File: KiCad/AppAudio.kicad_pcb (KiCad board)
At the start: 2 copper layers, 60 x 62 mm, 34 parts, among them P1 WRITER-VCC, Q1 Q_NMOS_SGD, SW1 SW_PUSH, SW2 SW_PUSH, U1 TWE_LITE_SMD, U2 LMC6062, U3 HT82V739

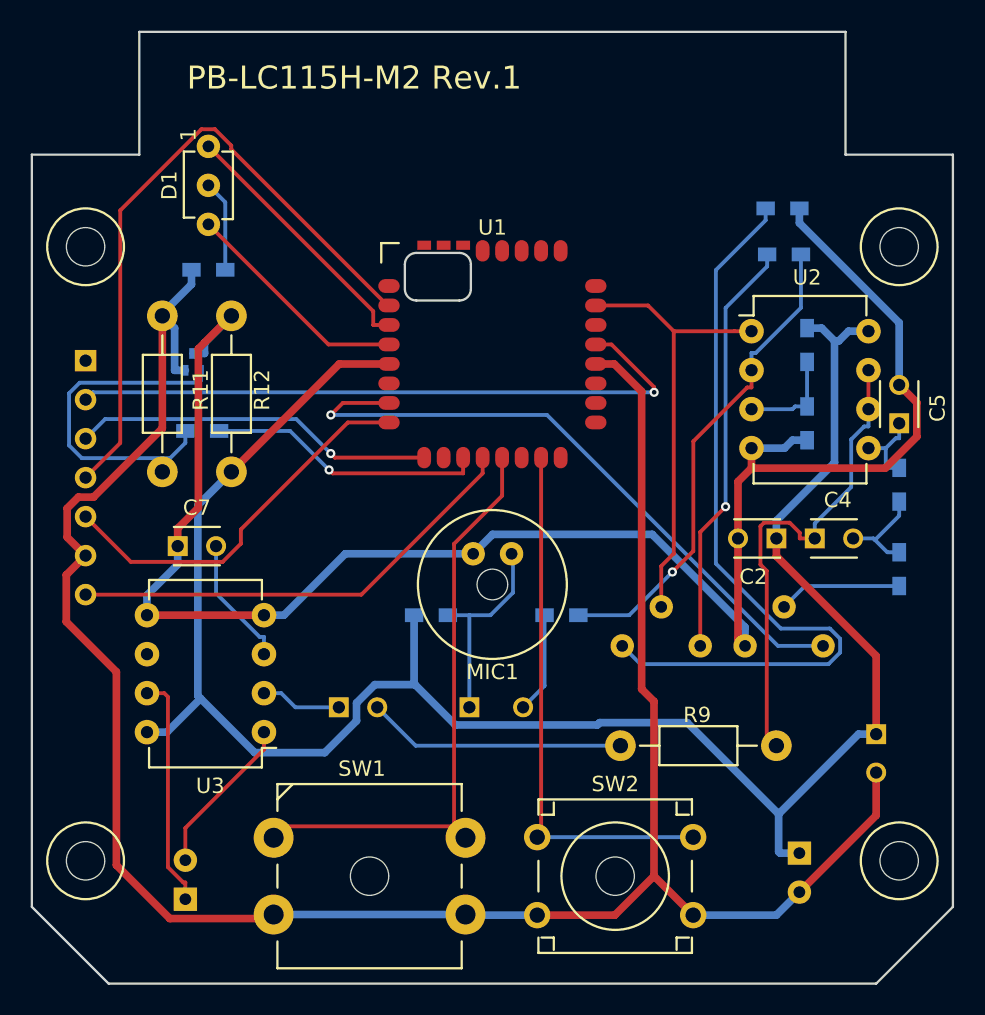
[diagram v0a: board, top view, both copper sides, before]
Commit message: Connect CE# to DO3.
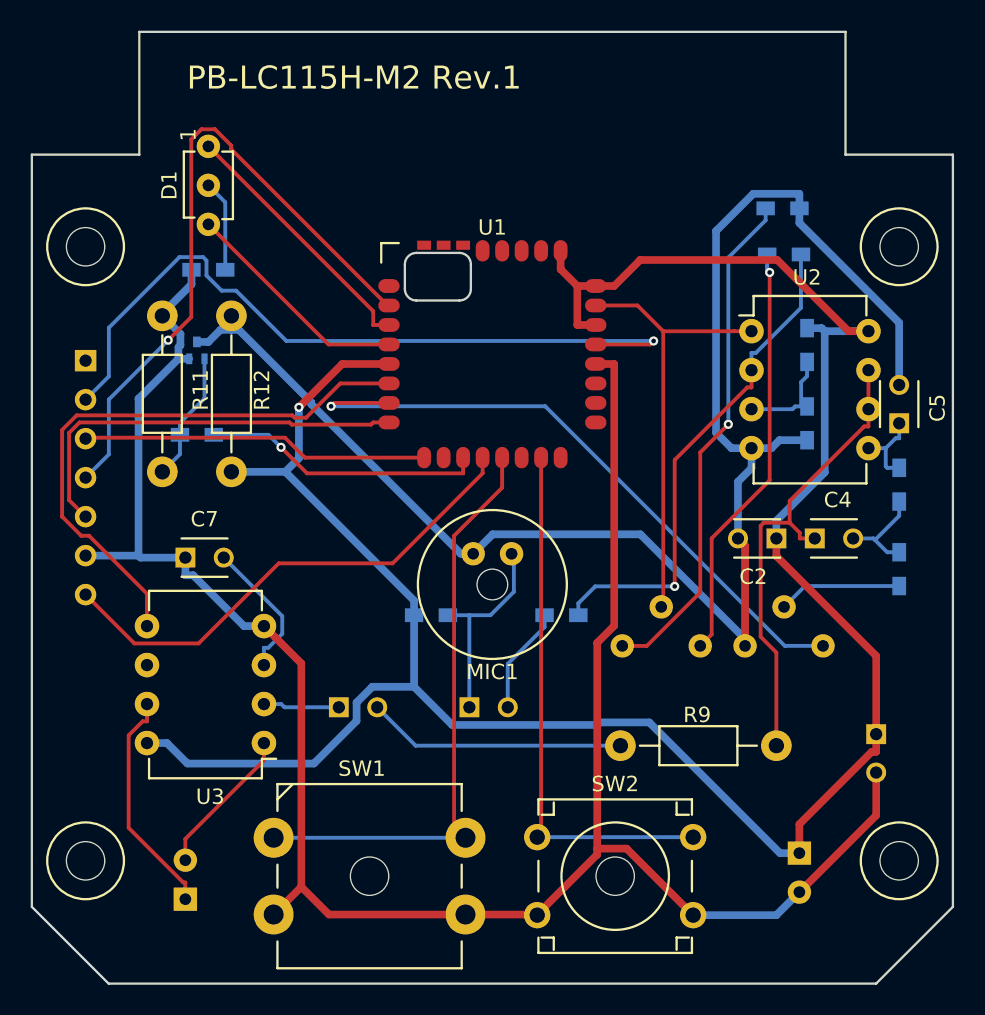
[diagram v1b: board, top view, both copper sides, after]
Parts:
- C1: value 33u -> 22u; footprint Capacitors_ThroughHole:C_Radial_D8_L11.5_P3.5 -> Capacitors_ThroughHole:C_Radial_D6.3_L11.2_P2.5
- R11, R12: value 2.2M -> 100k
- U2: value LMC6062 -> NJM13404
- moved C7 0.90 mm to (80.0, 100.2)
- moved Q1 0.79 mm to (80.8, 86.8)
- moved U3 0.71 mm to (85.1, 112.3)
- moved R10 0.43 mm to (80.8, 92.2)
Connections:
- C7 pad 1: VSS -> GND
- U1 pad 22: Net-(U1-Pad22) -> VCC
- U1 pad 24: Net-(U1-Pad24) -> VCC
- U1 pad 25: Net-(U1-Pad25) -> VCC
- U1 pad 6: Net-(U1-Pad6) -> /DO3
- U3 pad 4: VSS -> GND
- U3 pad 5: VSS -> /DO3
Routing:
- net /DO3: track 0.00 -> 38.0 mm
- net VCC: track 130.0 -> 155.4 mm, vias 0 -> 1
- net Net-(R6-Pad2): track 50.5 -> 33.3 mm, vias 0 -> 1
- net VSS: track 117.5 -> 101.6 mm
- net Net-(Q1-Pad2): track 23.0 -> 8.50 mm
- net /RST: track 42.5 -> 49.4 mm
- net GND: track 144.0 -> 137.2 mm
- net /CFG: track 30.2 -> 32.8 mm
- net /TXD: track 25.3 -> 27.1 mm
- net Net-(R2-Pad1): track 31.8 -> 32.9 mm
- net /RXD: track 23.6 -> 22.6 mm, vias 1 -> 0
- net /VREF: track 8.50 -> 9.24 mm
- net /OUTN: track 10.5 -> 9.75 mm
- net /PRG: vias 0 -> 1

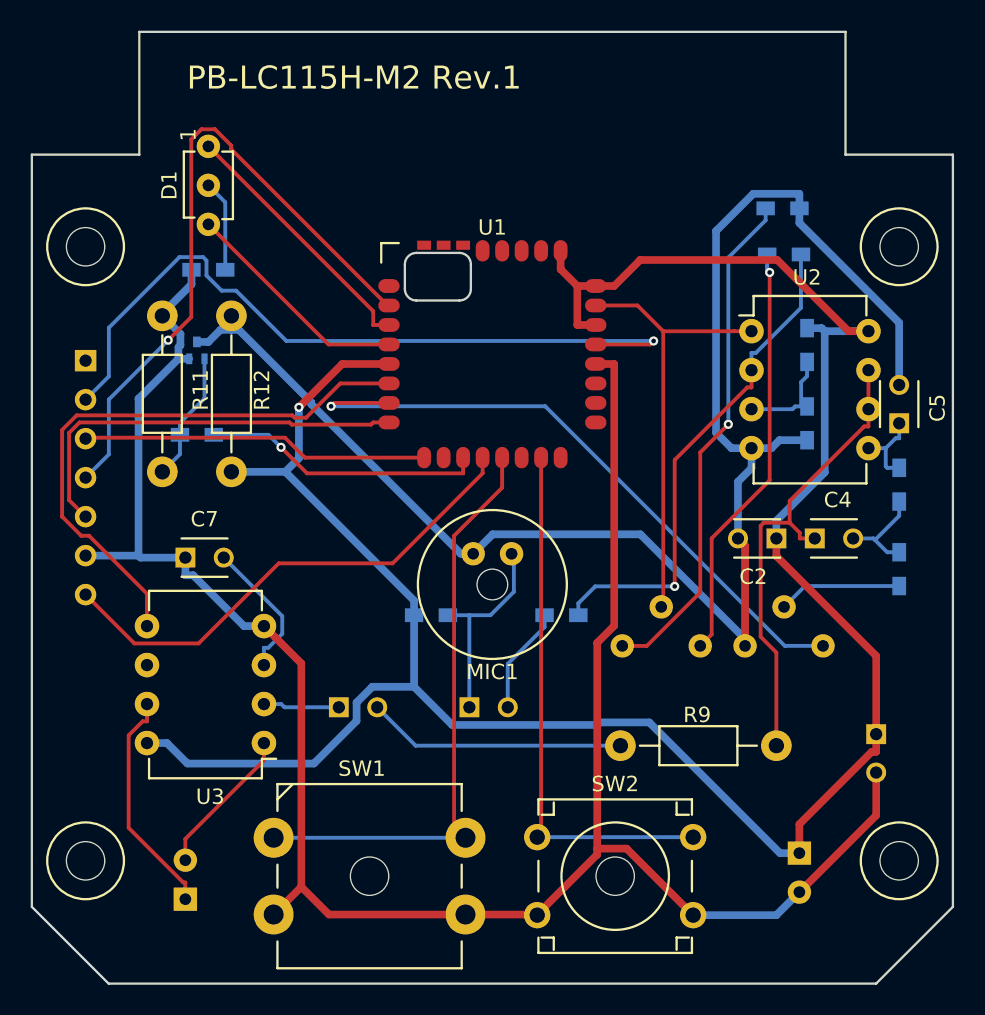
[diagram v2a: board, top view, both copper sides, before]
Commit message: Replaced some SMD registers.
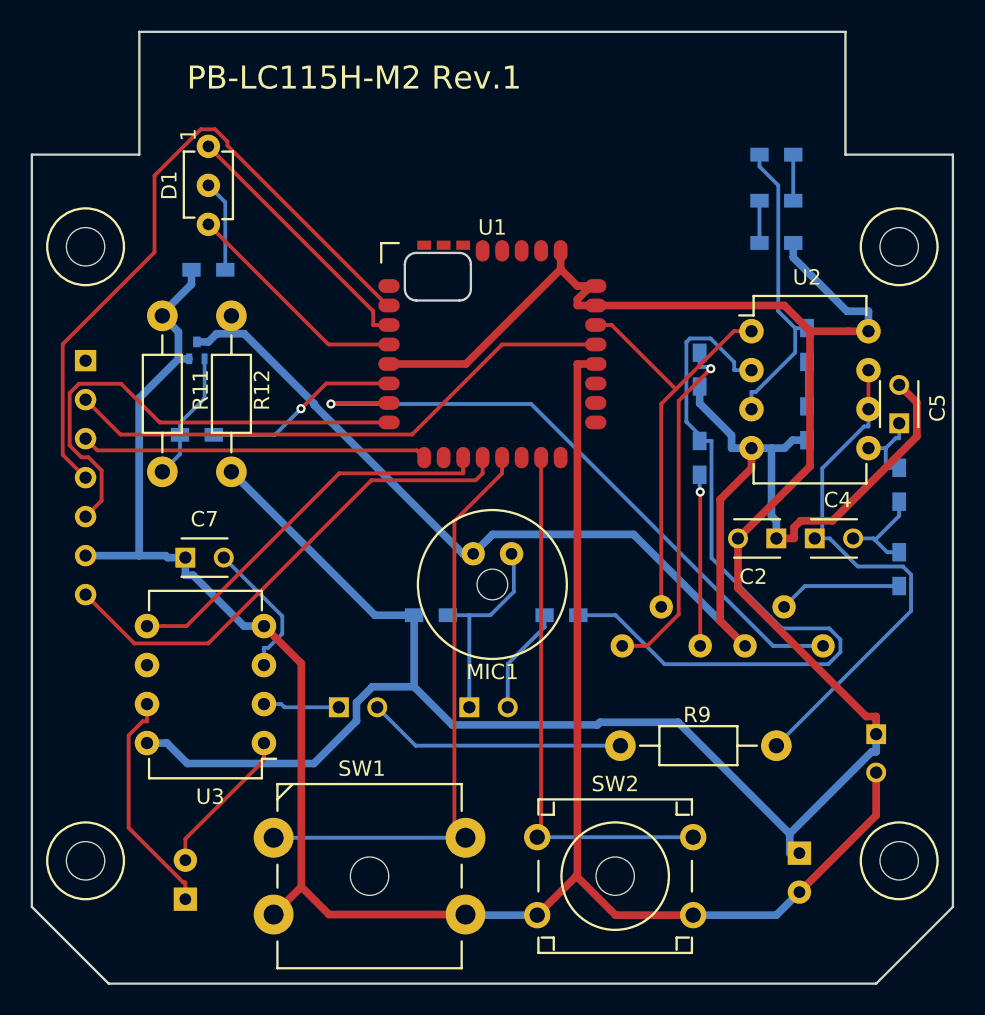
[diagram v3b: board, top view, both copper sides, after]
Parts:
- added R14: 510, Resistors_SMD:R_0603_HandSoldering, B.Cu at (118.5, 79.8)
- added R15: 510, Resistors_SMD:R_0603_HandSoldering, B.Cu at (118.5, 77.0)
- added R16: 510, Resistors_SMD:R_0603_HandSoldering, B.Cu at (118.5, 74.0)
- R10, R13, R4: value 1k -> 510
- R11: value 100k -> 1M
- R3: value 1.5k -> 510
- R9: value 100 -> 22k
- moved R5 14.3 mm to (113.5, 93.8), turned to 90 degrees
- moved R6 11.8 mm to (113.5, 88.0), turned to 270 degrees
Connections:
- C2 pad 1: VCC -> VSS
- C2 pad 2: VSS -> VCC
- R3 pad 1: VCC -> Net-(R16-Pad2)
- R6 pad 1: VSS -> Net-(R6-Pad1)
- R6 pad 2: Net-(R6-Pad2) -> VSS
- U1 pad 11: Net-(R10-Pad1) -> /DO4
- U1 pad 22: VCC -> Net-(U1-Pad22)
- U1 pad 23: Net-(U1-Pad23) -> VCC
- U1 pad 6: /DO3 -> Net-(R10-Pad1)
- U2 pad 1: Net-(U1-Pad23) -> Net-(U1-Pad22)
- U2 pad 3: Net-(R3-Pad2) -> Net-(R16-Pad2)
- U3 pad 5: /DO3 -> /DO4
- VR1 pad 2: Net-(U1-Pad23) -> Net-(U1-Pad22)
- VR1 pad 3: Net-(R6-Pad2) -> Net-(R6-Pad1)
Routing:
- net /DO3: track 38.0 -> 0.00 mm
- net Net-(R6-Pad2): track 33.3 -> 0.00 mm, vias 1 -> 0
- net Net-(U1-Pad23): track 28.9 -> 0.00 mm
- net Net-(U1-Pad22): track 0.00 -> 28.0 mm
- net /DO4: track 0.00 -> 25.7 mm
- net Net-(R6-Pad1): track 0.00 -> 23.1 mm, vias 0 -> 1
- net Net-(R16-Pad2): track 0.00 -> 19.7 mm
- net Net-(R2-Pad1): track 32.9 -> 51.0 mm, vias 1 -> 0
- net Net-(R5-Pad1): track 27.4 -> 11.2 mm
- net /RST: track 49.4 -> 36.6 mm, vias 1 -> 0
- net VSS: track 101.6 -> 93.2 mm
- net Net-(R10-Pad1): track 18.3 -> 12.8 mm
- net VCC: track 155.4 -> 160.4 mm, vias 1 -> 0
- net /TXD: track 27.1 -> 31.7 mm
- net Net-(R3-Pad2): track 6.76 -> 2.90 mm
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
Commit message: Assign LED1 as TX indicator.
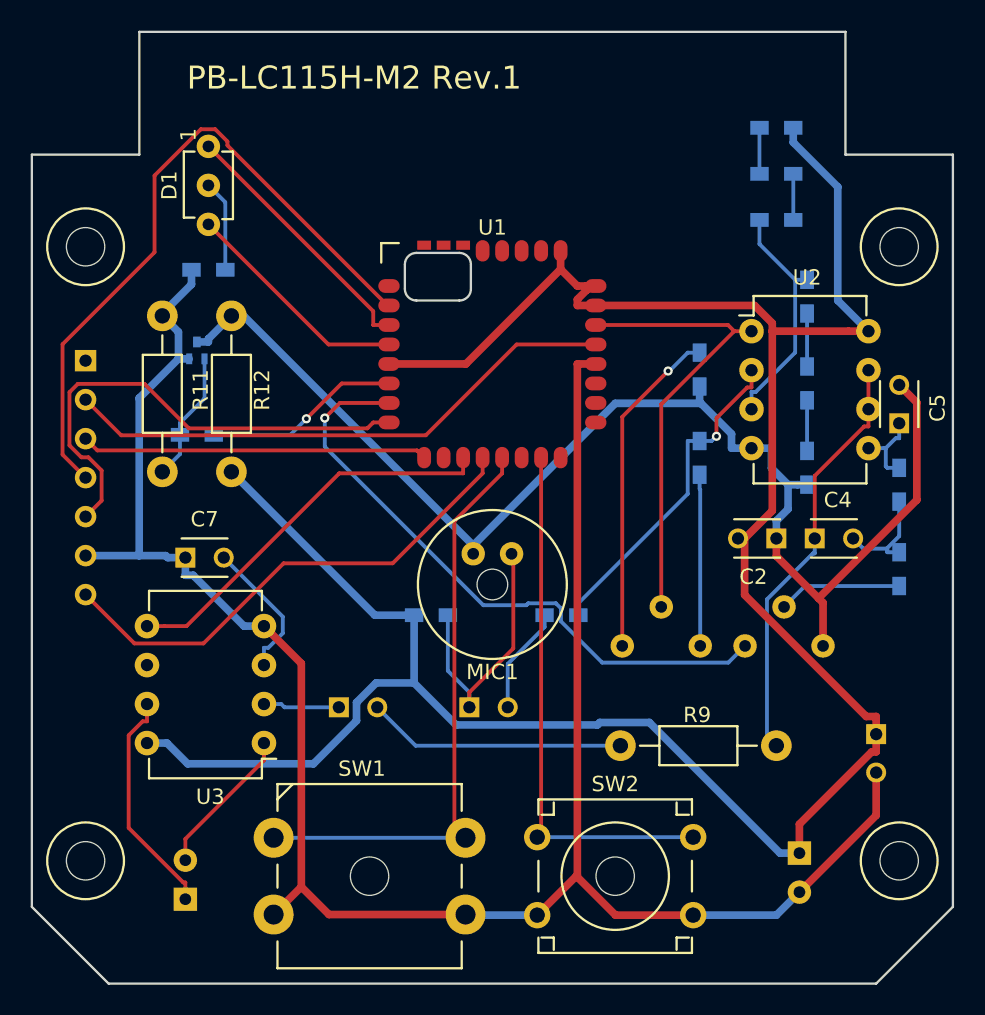
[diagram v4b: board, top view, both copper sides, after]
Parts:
- added R17: 510, Resistors_SMD:R_0603_HandSoldering, B.Cu at (118.5, 72.2)
- moved R14 4.03 mm to (120.5, 83.2), turned to 270 degrees
- moved R4 2.90 mm to (120.5, 94.4)
- moved R3 2.50 mm to (120.5, 88.9)
- moved R15 1.25 mm to (118.5, 78.2), turned to 180 degrees
- moved R16 1.25 mm to (118.5, 75.2), turned to 0 degrees
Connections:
- net /DO4 renamed /CE#
- R14 pad 1: VCC -> Net-(R14-Pad1)
- R15 pad 1: Net-(R14-Pad2) -> Net-(R15-Pad1)
- R15 pad 2: Net-(R15-Pad2) -> Net-(R14-Pad1)
- R16 pad 1: Net-(R15-Pad2) -> Net-(R16-Pad1)
- R16 pad 2: Net-(R16-Pad2) -> Net-(R15-Pad1)
- R3 pad 1: Net-(R16-Pad2) -> Net-(R14-Pad2)
- U2 pad 3: Net-(R16-Pad2) -> Net-(R14-Pad1)
- VR2 pad 1: Net-(U1-Pad7) -> VSS
- VR2 pad 3: VSS -> Net-(U1-Pad7)
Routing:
- net Net-(R2-Pad1): track 51.0 -> 21.7 mm, vias 0 -> 1
- net Net-(R16-Pad2): track 19.7 -> 0.00 mm
- net Net-(R14-Pad1): track 0.00 -> 15.4 mm
- net VSS: track 93.2 -> 84.8 mm
- net Net-(C4-Pad1): track 34.4 -> 27.7 mm
- net VCC: track 160.4 -> 166.6 mm
- net Net-(C1-Pad1): track 13.5 -> 17.8 mm
- net Net-(R16-Pad1): track 0.00 -> 3.00 mm
- net Net-(R15-Pad2): track 3.00 -> 0.00 mm
- net Net-(R15-Pad1): track 0.00 -> 3.00 mm
- net Net-(U1-Pad22): track 28.0 -> 30.2 mm
- net Net-(U1-Pad7): track 42.4 -> 40.7 mm
- net Net-(R6-Pad1): track 23.1 -> 21.7 mm
- net Net-(R14-Pad2): track 2.75 -> 3.45 mm
- net Net-(R5-Pad1): vias 1 -> 0
